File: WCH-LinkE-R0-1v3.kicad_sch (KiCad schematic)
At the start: 38 parts, among them Q1 DMG1012UW-7, Q2 DMG1012UW-7, SW1 SKRPASE010, SW2 SKRPASE010, SW3 SKRPASE010

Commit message: Clean up symbols library
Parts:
- LED3, LED4: DigiKey (none) -> 846-CSL0902BT1TR-ND
- Q1, Q2: DigiKey (none) -> DMG1012UW-7DITR-ND; Farnell (none) -> 3127309; Mouser (none) -> 621-DMG1012UW-7
- SW1, SW2, SW3: DigiKey (none) -> 4809-SKRPADE010TR-ND; Farnell (none) -> 3261826; Mouser (none) -> 688-SKRPASE010
- TVS4, TVS5, TVS6: Farnell (none) -> 2777317; Mouser (none) -> 576-SP1007-01ETG
- U3: AliExpress (none) -> 1005004329064488
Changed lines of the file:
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@@
       (effects (font (size 1.27 1.27)) hide)
     )
-    (property "Datasheet" "" (at 123.19 90.17 0)
+    (property "Datasheet" "https://www.farnell.com/datasheets/2864500.pdf" (at 123.19 90.17 0)
       (effects (font (size 1.27 1.27)) hide)
     )
@@
     )
     (property "JLCPCB Part #" "C470427" (at 110.49 90.17 0)
+      (effects (font (size 1.27 1.27)) hide)
+    )
+    (property "DigiKey" "4809-SKRPADE010TR-ND" (at 111.76 90.17 0)
+      (effects (font (size 1.27 1.27)) hide)
+    )
+    (property "Farnell" "3261826" (at 109.22 90.17 0)
+      (effects (font (size 1.27 1.27)) hide)
+    )
+    (property "Mouser" "688-SKRPASE010" (at 106.68 90.17 0)
       (effects (font (size 1.27 1.27)) hide)
     )
@@
     )
     (property "Farnell" "3954417" (at 46.99 92.71 0)
+      (effects (font (size 1.27 1.27)) hide)
+    )
+    (property "DigiKey" "846-CSL0902BT1TR-ND" (at 34.29 92.71 0)
       (effects (font (size 1.27 1.27)) hide)
     )
@@
       (effects (font (size 1.27 1.27)) hide)
     )
+    (property "DigiKey" "846-CSL0902BT1TR-ND" (at 22.86 92.71 0)
+      (effects (font (size 1.27 1.27)) hide)
+    )
     (pin "1")
     (pin "2")
@@
       (effects (font (size 1.27 1.27)) (justify left) hide)
     )
+    (property "Farnell" "2777317" (at 88.9 78.74 0)
+      (effects (font (size 1.27 1.27)) hide)
+    )
+    (property "Mouser" "576-SP1007-01ETG" (at 88.9 81.28 0)
+      (effects (font (size 1.27 1.27)) hide)
+    )
     (pin "1")
     (pin "2")
@@
       (effects (font (size 1.27 1.27)) hide)
     )
+    (property "DigiKey" "DMG1012UW-7DITR-ND" (at 49.53 96.52 0)
+      (effects (font (size 1.27 1.27)) hide)
+    )
+    (property "Farnell" "3127309" (at 49.53 99.06 0)
+      (effects (font (size 1.27 1.27)) hide)
+    )
+    (property "Mouser" "621-DMG1012UW-7" (at 49.53 101.6 0)
+      (effects (font (size 1.27 1.27)) hide)
+    )
     (pin "3")
     (pin "1")
@@
       (effects (font (size 1.27 1.27)) hide)
     )
-    (property "Datasheet" "" (at 106.68 121.92 0)
+    (property "Datasheet" "https://www.farnell.com/datasheets/2864500.pdf" (at 106.68 121.92 0)
       (effects (font (size 1.27 1.27)) hide)
     )
@@
     )
     (property "JLCPCB Part #" "C470427" (at 93.98 121.92 0)
+      (effects (font (size 1.27 1.27)) hide)
+    )
+    (property "DigiKey" "4809-SKRPADE010TR-ND" (at 95.25 121.92 0)
+      (effects (font (size 1.27 1.27)) hide)
+    )
+    (property "Farnell" "3261826" (at 92.71 121.92 0)
+      (effects (font (size 1.27 1.27)) hide)
+    )
+    (property "Mouser" "688-SKRPASE010" (at 90.17 121.92 0)
       (effects (font (size 1.27 1.27)) hide)
     )
@@
       (effects (font (size 1.27 1.27)) (justify left) hide)
     )
+    (property "Farnell" "2777317" (at 72.39 110.49 0)
+      (effects (font (size 1.27 1.27)) hide)
+    )
+    (property "Mouser" "576-SP1007-01ETG" (at 72.39 113.03 0)
+      (effects (font (size 1.27 1.27)) hide)
+    )
     (pin "1")
     (pin "2")
@@
     (property "JLCPCB Part #" "C5123443" (at 171.45 39.37 0)
       (effects (font (size 1.27 1.27)) hide)
+    )
+    (property "AliExpress" "1005004329064488" (at 171.45 15.24 0)
+      (effects (font (size 1.27 1.27)) hide)
+    )
+    (property "DigiKey" "" (at 171.45 39.37 0)
+      (effects (font (size 1.27 1.27)))
+    )
+    (property "Farnell" "" (at 171.45 39.37 0)
+      (effects (font (size 1.27 1.27)))
+    )
+    (property "Mouser" "" (at 171.45 39.37 0)
+      (effects (font (size 1.27 1.27)))
     )
     (pin "20")
@@
       (effects (font (size 1.27 1.27)) hide)
     )
-    (property "Datasheet" "" (at 179.07 91.44 0)
+    (property "Datasheet" "https://www.farnell.com/datasheets/2864500.pdf" (at 179.07 91.44 0)
       (effects (font (size 1.27 1.27)) hide)
     )
@@
     )
     (property "JLCPCB Part #" "C470427" (at 166.37 91.44 0)
+      (effects (font (size 1.27 1.27)) hide)
+    )
+    (property "DigiKey" "4809-SKRPADE010TR-ND" (at 167.64 91.44 0)
+      (effects (font (size 1.27 1.27)) hide)
+    )
+    (property "Farnell" "3261826" (at 165.1 91.44 0)
+      (effects (font (size 1.27 1.27)) hide)
+    )
+    (property "Mouser" "688-SKRPASE010" (at 162.56 91.44 0)
       (effects (font (size 1.27 1.27)) hide)
     )
@@
       (effects (font (size 1.27 1.27)) (justify left) hide)
     )
+    (property "Farnell" "2777317" (at 152.4 80.01 0)
+      (effects (font (size 1.27 1.27)) hide)
+    )
+    (property "Mouser" "576-SP1007-01ETG" (at 152.4 82.55 0)
+      (effects (font (size 1.27 1.27)) hide)
+    )
     (pin "1")
     (pin "2")
@@
       (effects (font (size 1.27 1.27)) hide)
     )
+    (property "DigiKey" "" (at 125.73 92.71 0)
+      (effects (font (size 1.27 1.27)))
+    )
+    (property "Farnell" "" (at 125.73 92.71 0)
+      (effects (font (size 1.27 1.27)))
+    )
+    (property "Mouser" "" (at 125.73 92.71 0)
+      (effects (font (size 1.27 1.27)))
+    )
     (pin "1")
     (pin "2")
@@
       (effects (font (size 1.27 1.27)) hide)
     )
+    (property "DigiKey" "DMG1012UW-7DITR-ND" (at 38.1 96.52 0)
+      (effects (font (size 1.27 1.27)) hide)
+    )
+    (property "Farnell" "3127309" (at 38.1 99.06 0)
+      (effects (font (size 1.27 1.27)) hide)
+    )
+    (property "Mouser" "621-DMG1012UW-7" (at 38.1 101.6 0)
+      (effects (font (size 1.27 1.27)) hide)
+    )

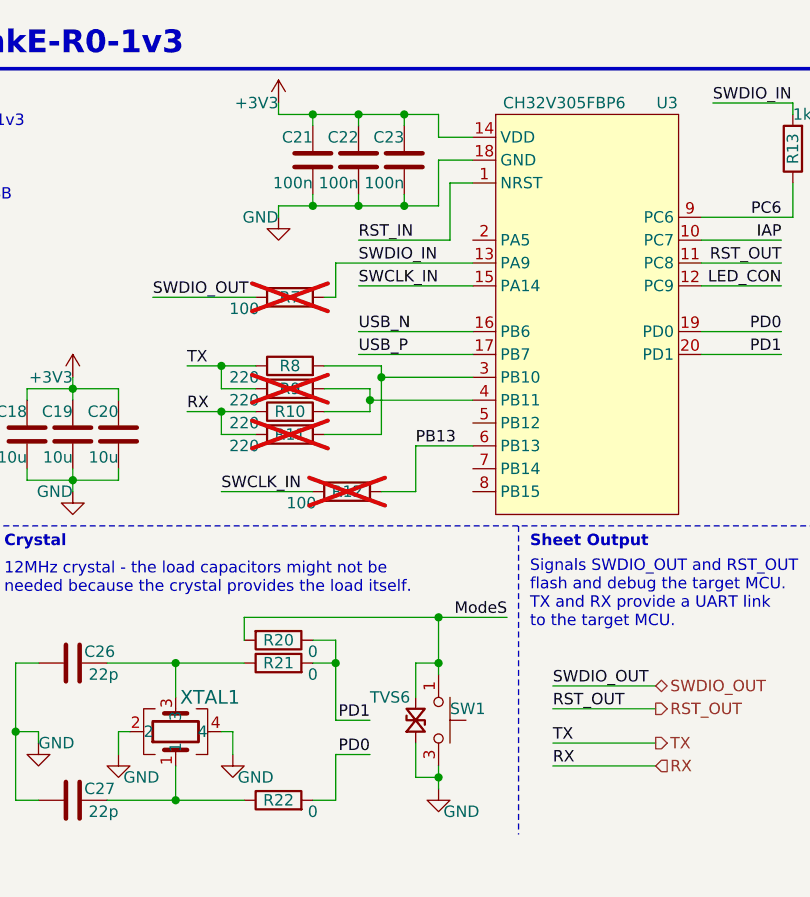
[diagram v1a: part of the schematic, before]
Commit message: Prefix each symbol name in library - eg. 'D_', 'CONN_', 'IC_', ...
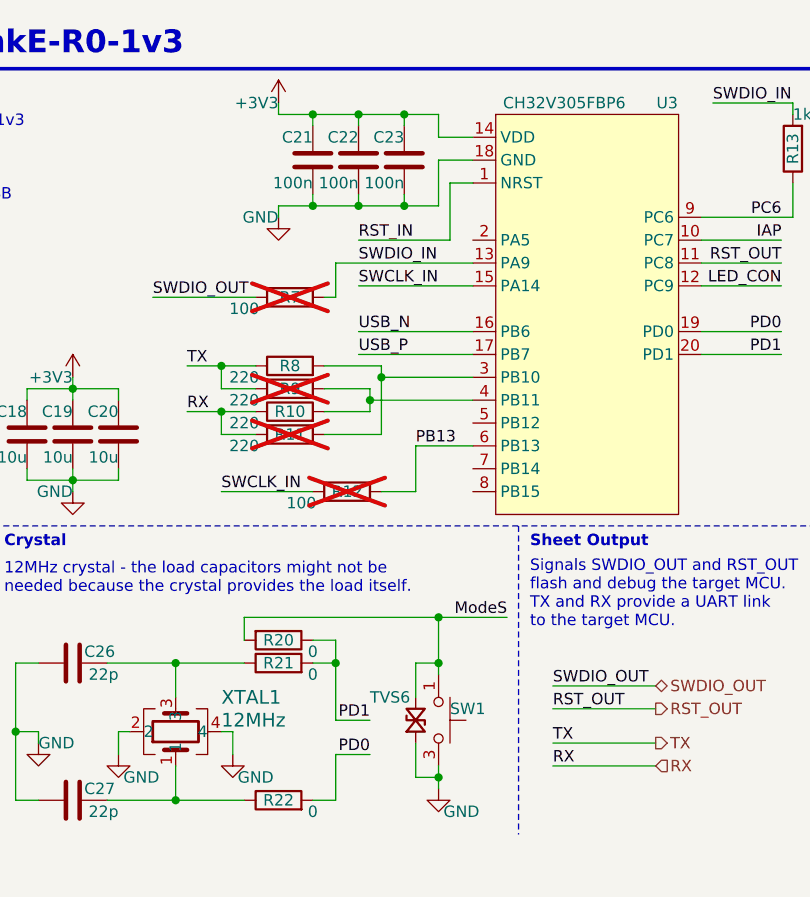
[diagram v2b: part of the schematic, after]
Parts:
- SW1, SW2, SW3: value SKRPASE010 -> 16V 50mA; symbol Tiny_Scarab:SKRPASE010 -> Tiny_Scarab:SW_SKRPASE010; SPN 4809-SKRPADE010TR-ND -> (none); Supplier DigiKey -> (none)
- U3: value ~ -> CH32V305FBP6; symbol Tiny_Scarab:CH32V305FBP6 -> Tiny_Scarab:IC_CH32V305FBP6; SPN 1005004329064488 -> (none); Supplier AliExpress -> (none)
- XTAL1: value SX5B12.000F2020F30 -> 12MHz; symbol Tiny_Scarab:SX5B12.000F2020F30 -> Tiny_Scarab:XTAL_SX5B12.000F2020F30

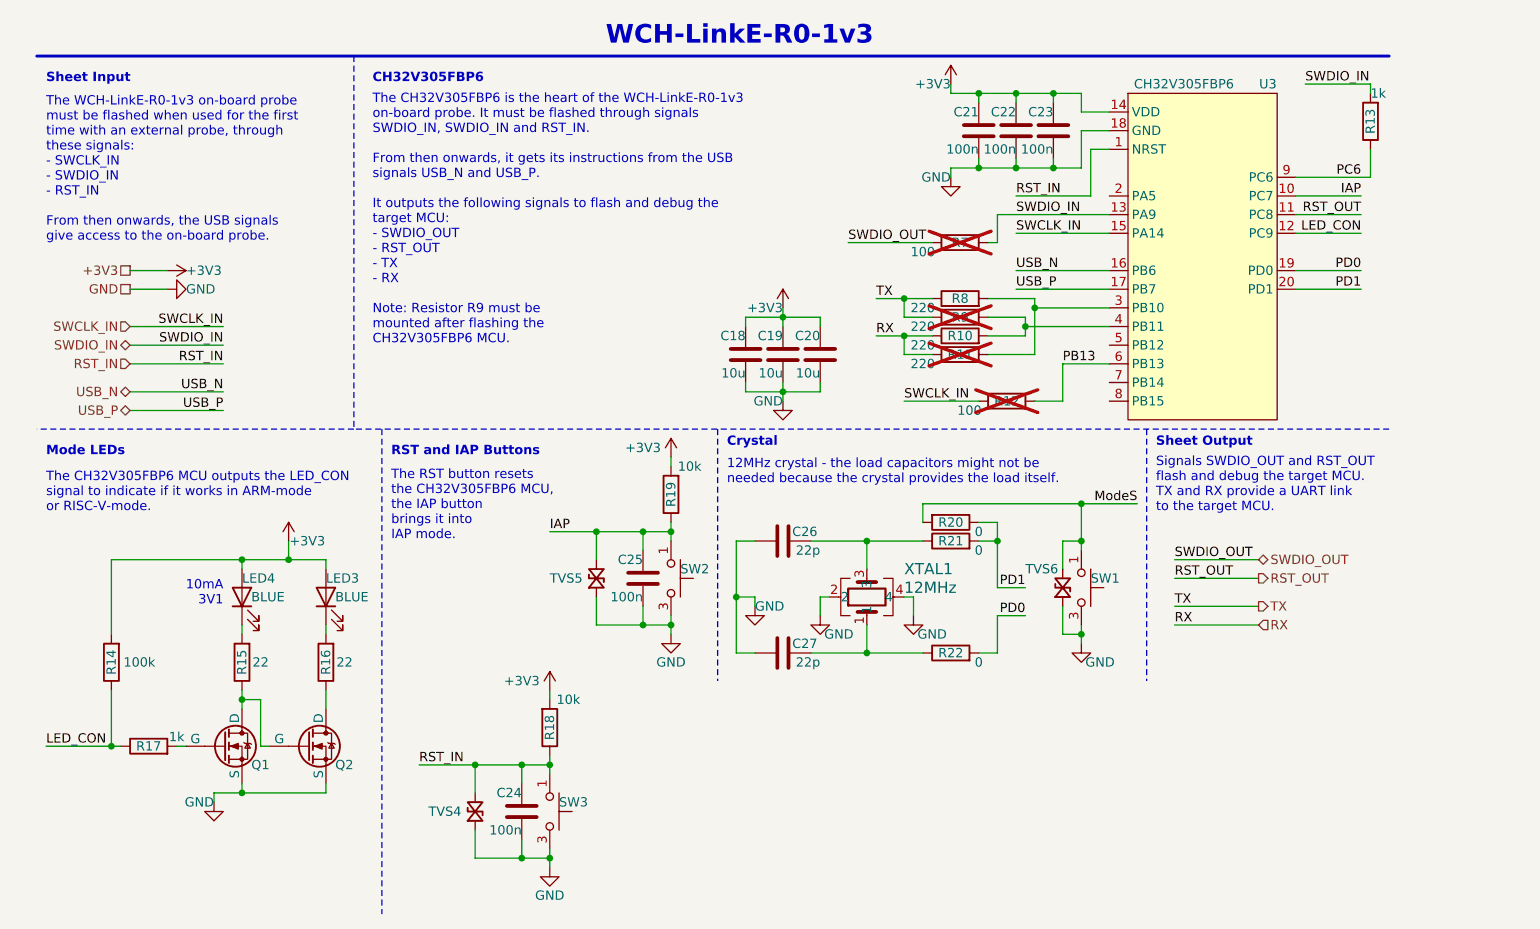
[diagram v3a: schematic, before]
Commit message: Rename net 'RST_OUT' into 'RST_CH32V003'
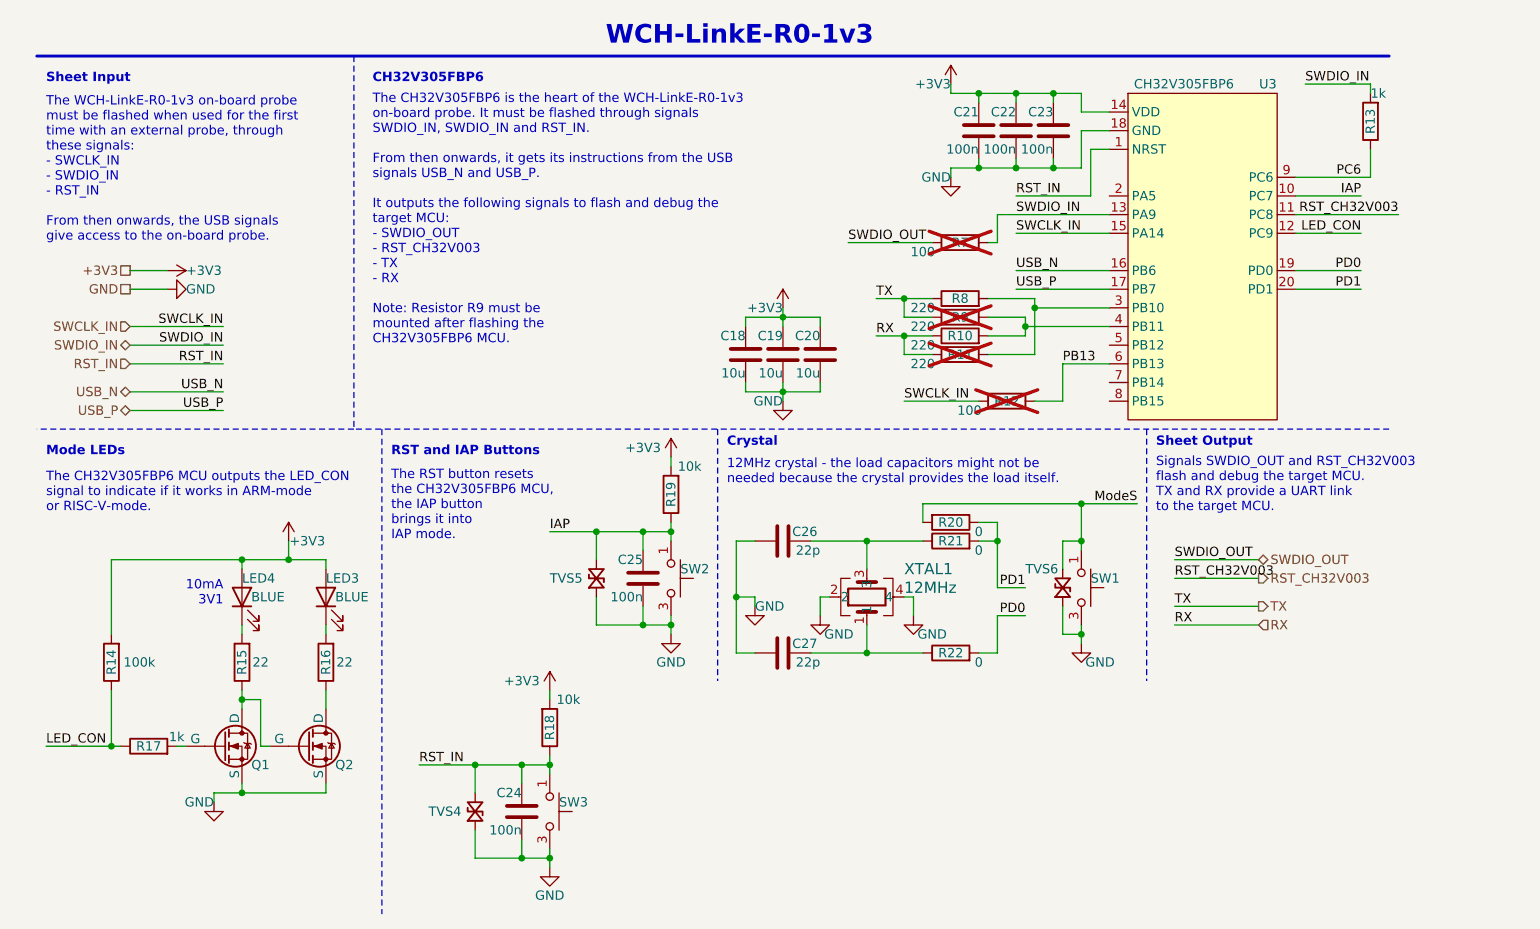
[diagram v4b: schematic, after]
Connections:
- net RST_OUT renamed RST_CH32V003
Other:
- note added: "Signals SWDIO_OUT and RST_CH32V003 flash and debug the target MCU. TX and RX provide a UART link to the target MCU."
- note added: "The CH32V305FBP6 is the heart of the WCH-LinkE-R0-1v3 on-board probe. It must be flashed through signals SWDIO_IN, SWDIO_IN and RST_IN. From then onwards, it gets its instructions from the USB signals USB_N and USB_P. It outputs the following signals to flash and debug the target MCU: - SWDIO_OUT - RST_CH32V003 - TX - RX Note: Resistor R9 must be mounted after flashing the CH32V305FBP6 MCU."
- note removed: "Signals SWDIO_OUT and RST_OUT flash and debug the target MCU. TX and RX provide a UART link to the target MCU."
- note removed: "The CH32V305FBP6 is the heart of the WCH-LinkE-R0-1v3 on-board probe. It must be flashed through signals SWDIO_IN, SWDIO_IN and RST_IN. From then onwards, it gets its instructions from the USB signals USB_N and USB_P. It outputs the following signals to flash and debug the target MCU: - SWDIO_OUT - RST_OUT - TX - RX Note: Resistor R9 must be mounted after flashing the CH32V305FBP6 MCU."
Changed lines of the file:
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@@
     (stroke (width 0) (type default))
   )
-  (wire (pts (xy 184.15 40.64) (xy 193.04 40.64))
+  (wire (pts (xy 184.15 40.64) (xy 198.12 40.64))
     (stroke (width 0) (type default))
   )
@@
     (effects (font (size 1.27 1.27)) (justify left bottom))
   )
-  (text "Signals SWDIO_OUT and RST_OUT\nflash and debug the target MCU.\nTX and RX provide a UART link\nto the target MCU."
+  (text "Signals SWDIO_OUT and RST_CH32V003\nflash and debug the target MCU.\nTX and RX provide a UART link\nto the target MCU."
     (at 165.1 81.28 0)
     (effects (font (size 1.27 1.27)) (justify left bottom))
@@
     (effects (font (size 1.27 1.27)) (justify left bottom))
   )
-  (text "The CH32V305FBP6 is the heart of the WCH-LinkE-R0-1v3\non-board probe. It must be flashed through signals\nSWDIO_IN, SWDIO_IN and RST_IN.\n\nFrom then onwards, it gets its instructions from the USB\nsignals USB_N and USB_P.\n\nIt outputs the following signals to flash and debug the\ntarget MCU:\n- SWDIO_OUT\n- RST_OUT\n- TX\n- RX\n\nNote: Resistor R9 must be\nmounted after flashing the\nCH32V305FBP6 MCU."
+  (text "The CH32V305FBP6 is the heart of the WCH-LinkE-R0-1v3\non-board probe. It must be flashed through signals\nSWDIO_IN, SWDIO_IN and RST_IN.\n\nFrom then onwards, it gets its instructions from the USB\nsignals USB_N and USB_P.\n\nIt outputs the following signals to flash and debug the\ntarget MCU:\n- SWDIO_OUT\n- RST_CH32V003\n- TX\n- RX\n\nNote: Resistor R9 must be\nmounted after flashing the\nCH32V305FBP6 MCU."
     (at 58.42 58.42 0)
     (effects (font (size 1.27 1.27)) (justify left bottom))
@@
     (effects (font (size 1.27 1.27)) (justify right bottom))
   )
-  (label "RST_OUT" (at 167.64 90.17 0) (fields_autoplaced)
+  (label "RST_CH32V003" (at 167.64 90.17 0) (fields_autoplaced)
     (effects (font (size 1.27 1.27)) (justify left bottom))
   )
@@
     (effects (font (size 1.27 1.27)) (justify left bottom))
   )
-  (label "RST_OUT" (at 193.04 40.64 180) (fields_autoplaced)
+  (label "RST_CH32V003" (at 198.12 40.64 180) (fields_autoplaced)
     (effects (font (size 1.27 1.27)) (justify right bottom))
   )
@@
     (effects (font (size 1.27 1.27)) (justify right))
   )
-  (hierarchical_label "RST_OUT" (shape output) (at 179.07 90.17 0) (fields_autoplaced)
+  (hierarchical_label "RST_CH32V003" (shape output) (at 179.07 90.17 0) (fields_autoplaced)
     (effects (font (size 1.27 1.27)) (justify left))
   )
